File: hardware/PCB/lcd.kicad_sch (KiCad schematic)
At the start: 67 parts, among them U13 TPS923650, U14 TSC2013QRSARQ1

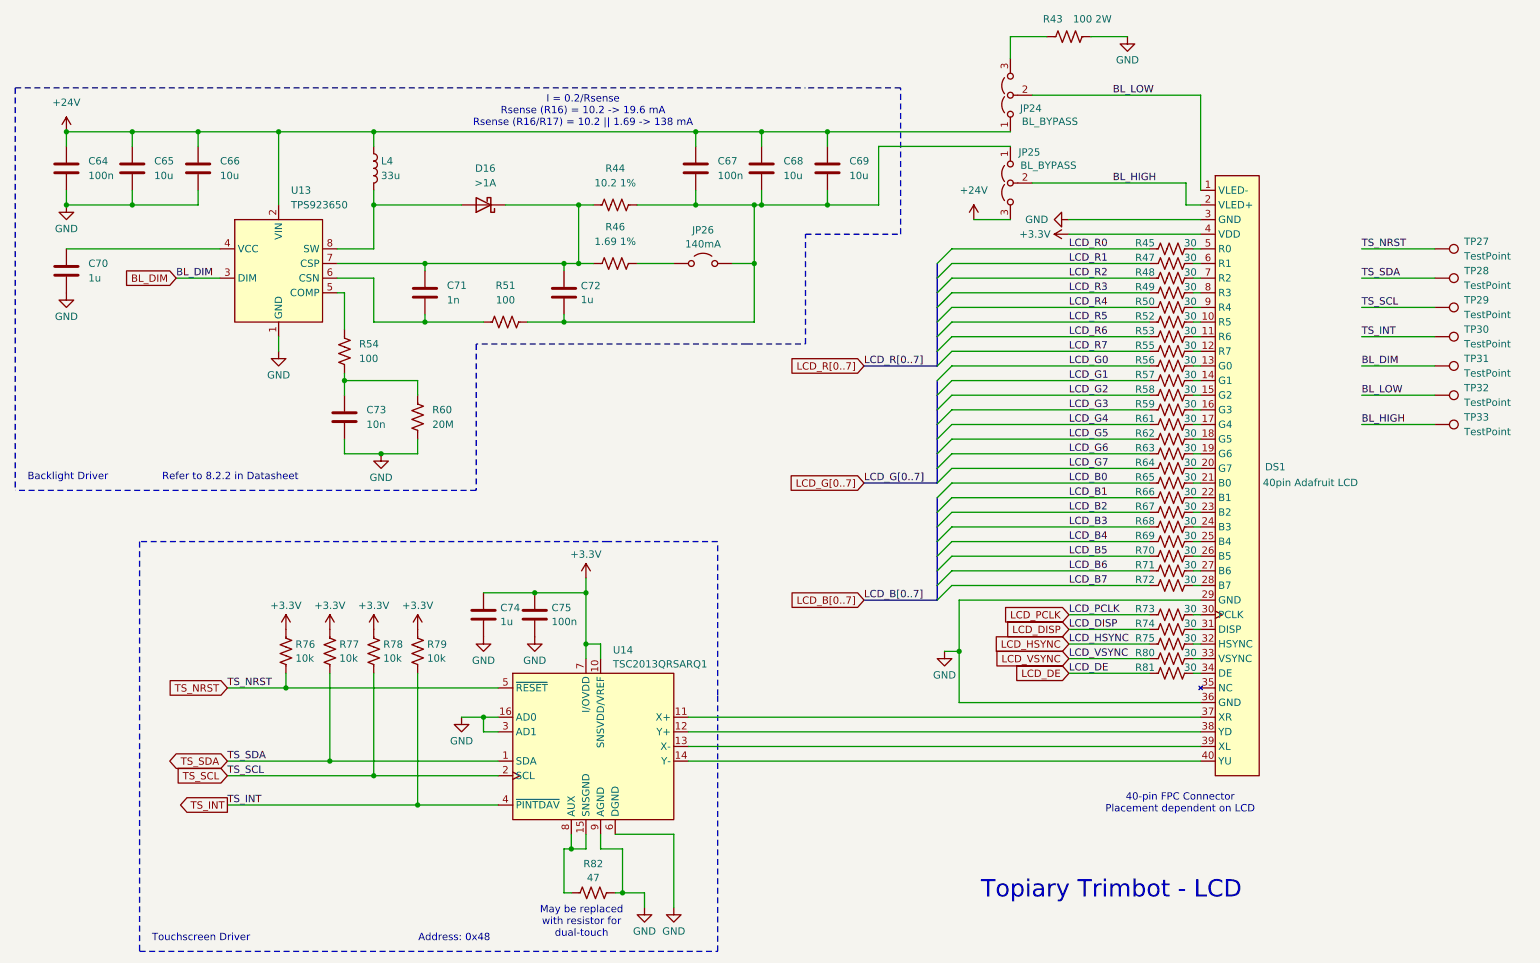
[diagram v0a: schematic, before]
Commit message: Finish first pass placement of parts on PCB, several updates and fixes to schematic included
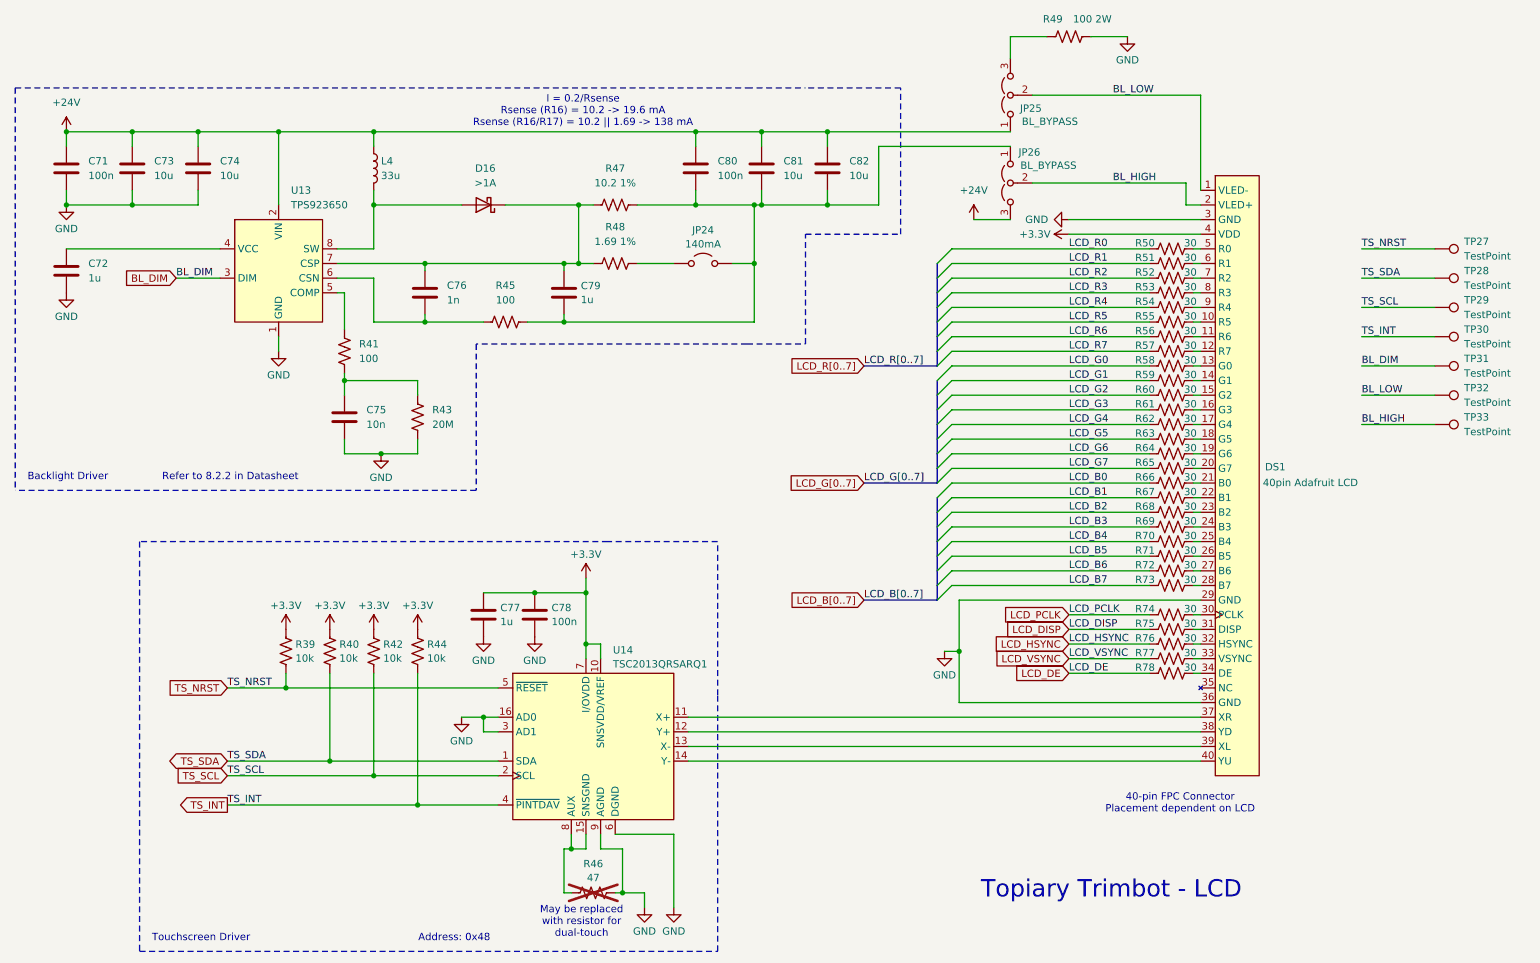
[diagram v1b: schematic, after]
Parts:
- DS1: footprint Connector_FFC-FPC:Hirose_FH12-40S-0.5SH_1x40-1MP_P0.50mm_Horizontal -> CustomFootprints:Hirose_FH12A-40S-0.5SH_1x40-1MP_P0.50mm_Horizontal
- R46: renamed from R82; now not fitted
- renumbered C64 to C71, C70 to C72, C65 to C73, C66 to C74, C73 to C75, C71 to C76, C74 to C77, C75 to C78, C72 to C79, C67 to C80, C68 to C81, C69 to C82, JP26 to JP24, JP24 to JP25, JP25 to JP26, R76 to R39, R77 to R40, R54 to R41, R78 to R42, R60 to R43, R79 to R44, R51 to R45, R44 to R47, R46 to R48, R43 to R49, R45 to R50, R47 to R51, R48 to R52, R49 to R53, R50 to R54, R52 to R55, R53 to R56, R55 to R57, R56 to R58, R57 to R59, R58 to R60, R59 to R61, R61 to R62, R62 to R63, R63 to R64, R64 to R65, R65 to R66, R66 to R67, R67 to R68, R68 to R69, R69 to R70, R70 to R71, R71 to R72, R72 to R73, R73 to R74, R74 to R75, R75 to R76, R80 to R77, R81 to R78

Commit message: Started routing
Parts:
- R46: value 47 -> 0; now fitted
- U13: footprint Package_SO:HVSSOP-8-1EP_3x3mm_P0.65mm_EP1.57x1.89mm -> CustomFootprints:TPS923650_VSSOP8
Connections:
- net GND: now also U13.9 (EP), U14.17 (EP)
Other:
- note added: "May be replaced with 47R for dual-touch"
- note removed: "May be replaced with resistor for dual-touch"

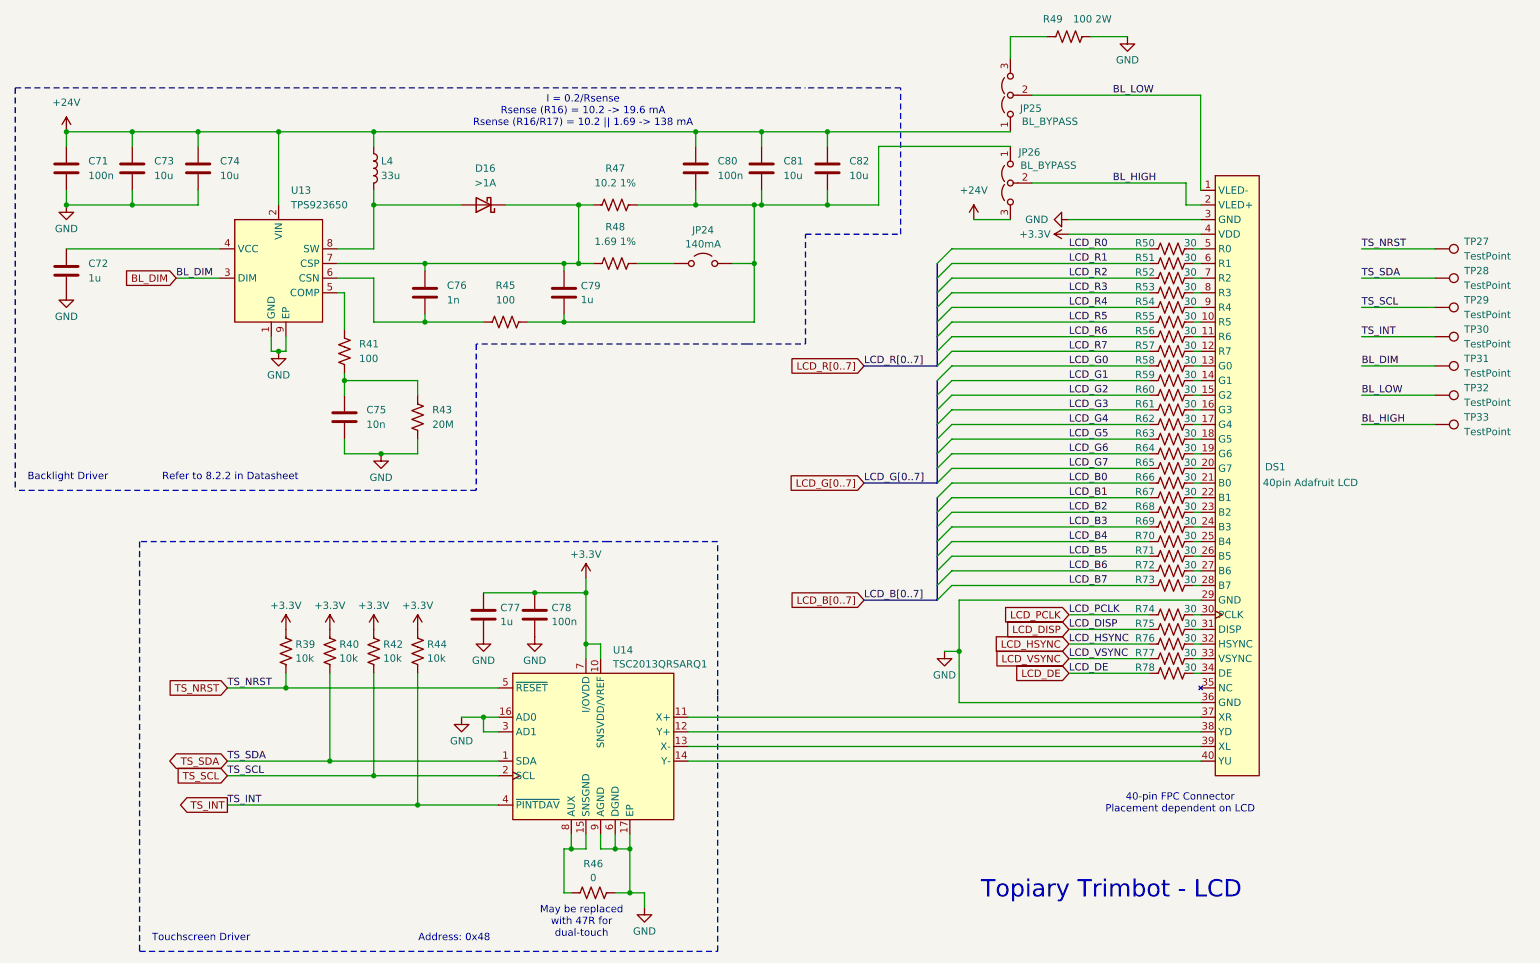
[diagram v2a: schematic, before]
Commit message: Continue layout, including swapping to linear BL driver
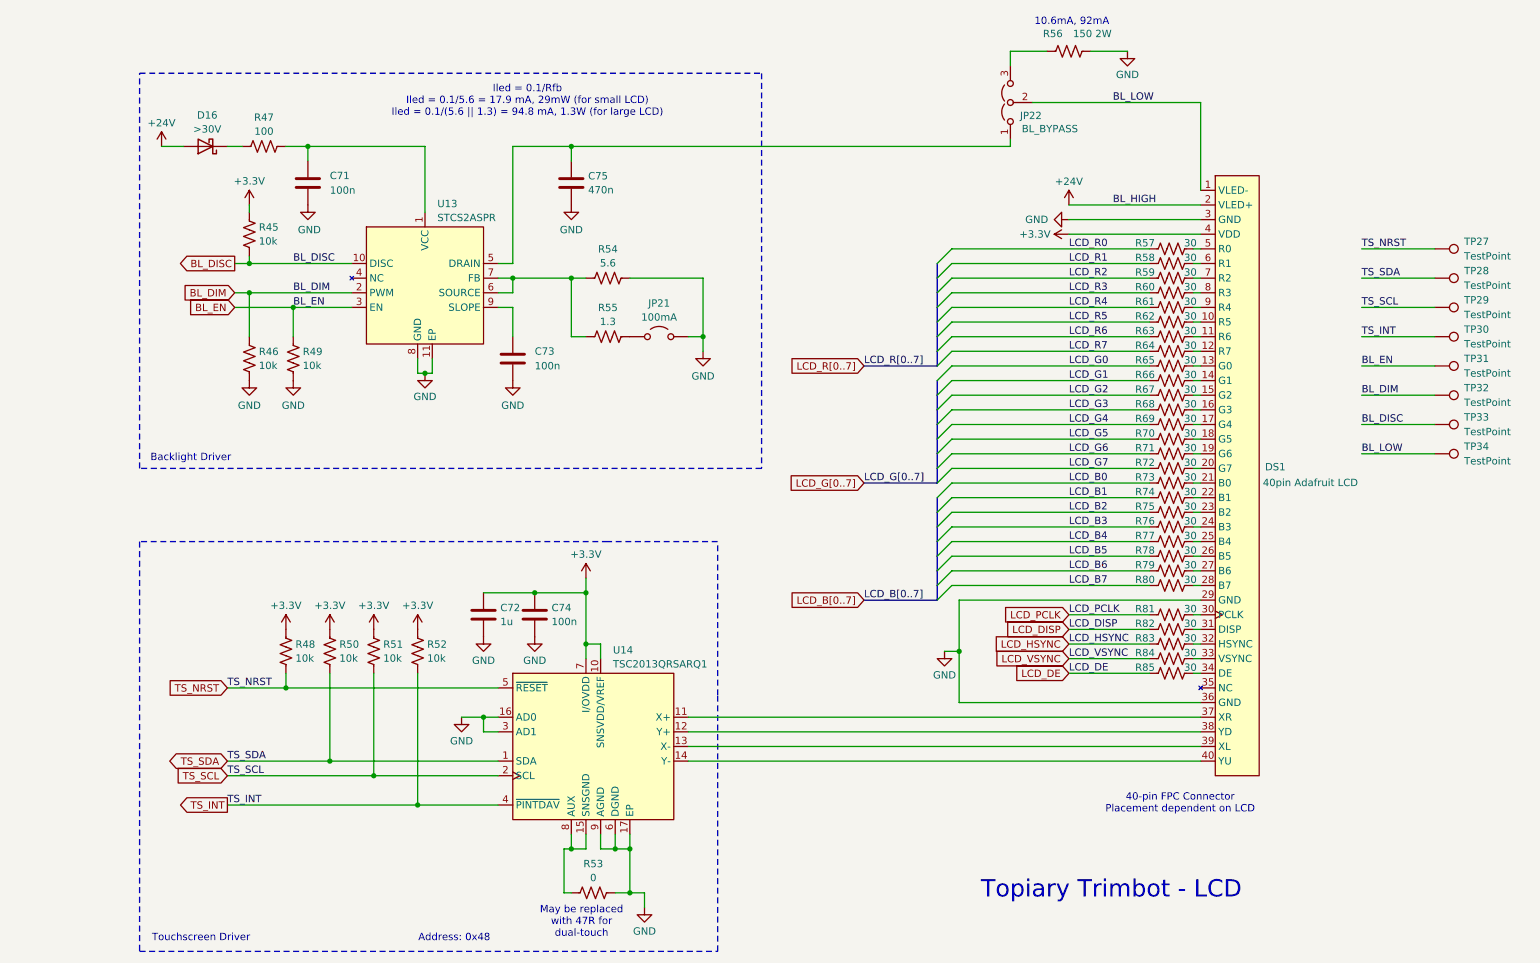
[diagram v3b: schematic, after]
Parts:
- removed C72, C79: 1u, Capacitor_SMD:C_0603_1608Metric, symbol Device:C
- removed C74, C81: 10u, Capacitor_SMD:C_0805_2012Metric, symbol Device:C
- removed C75: 10n, Capacitor_SMD:C_0603_1608Metric, symbol Device:C
- removed C76: 1n, Capacitor_SMD:C_0603_1608Metric, symbol Device:C
- removed C80: 100n, Capacitor_SMD:C_0603_1608Metric, symbol Device:C
- removed JP26: BL_BYPASS, Connector_PinHeader_2.54mm:PinHeader_1x03_P2.54mm_Vertical, symbol Jumper:Jumper_3_Open
- removed L4: 33u, Inductor_SMD:L_Bourns_SRR1208_12.7x12.7mm, symbol Device:L
- removed R41: 100, Resistor_SMD:R_0603_1608Metric, symbol Device:R_US
- removed R43: 20M, Resistor_SMD:R_0603_1608Metric, symbol Device:R_US
- removed R48: 1.69 1%, Resistor_SMD:R_0805_2012Metric, symbol Device:R_US
- removed TP33: TestPoint, TestPoint:TestPoint_Pad_D1.5mm, symbol Connector:TestPoint
- removed U13: TPS923650, CustomFootprints:TPS923650_VSSOP8, symbol CustomSymbols:TPS923650
- added R46, R49: 10k, Resistor_SMD:R_0805_2012Metric, symbol Device:R_US
- added R54: 5.6, Resistor_SMD:R_0805_2012Metric, symbol Device:R_US
- added R55: 1.3, Resistor_SMD:R_0805_2012Metric, symbol Device:R_US
- added TP31, TP32: TestPoint, TestPoint:TestPoint_Pad_D1.5mm, symbol Connector:TestPoint
- added U13: STCS2ASPR, CustomFootprints:STM_PowerSO-10, symbol CustomSymbols:STCS2ASPR
- C72: renamed from C77; footprint Capacitor_SMD:C_0603_1608Metric -> Capacitor_SMD:C_0805_2012Metric
- C73: value 10u -> 100n; footprint Capacitor_SMD:C_0805_2012Metric -> Capacitor_SMD:C_0603_1608Metric
- C75: renamed from C82; value 10u -> 470n
- D16: value >1A -> >30V; footprint Diode_SMD:D_SMB -> Diode_SMD:D_SOD-123; MANUFACTURER (none) -> STM; Manufacturer_Part_Number B280-13-F -> BAT46ZFILM
- JP21: renamed from JP24; value 140mA -> 100mA
- R45: value 100 -> 10k; footprint Resistor_SMD:R_0603_1608Metric -> Resistor_SMD:R_0805_2012Metric
- R47: value 10.2 1% -> 100
- R53: renamed from R46; footprint Resistor_SMD:R_0805_2012Metric_Pad1.20x1.40mm_HandSolder -> Resistor_SMD:R_0805_2012Metric
- R56: renamed from R49; value 100 2W -> 150 2W; Manufacturer_Part_Number AC05000001000JAC00 -> AC05000001507JAC00
- renumbered C78 to C74, JP25 to JP22, R39 to R48, R40 to R50, R42 to R51, R44 to R52, R50 to R57, R51 to R58, R52 to R59, R53 to R60, R54 to R61, R55 to R62, R56 to R63, R57 to R64, R58 to R65, R59 to R66, R60 to R67, R61 to R68, R62 to R69, R63 to R70, R64 to R71, R65 to R72, R66 to R73, R67 to R74, R68 to R75, R69 to R76, R70 to R77, R71 to R78, R72 to R79, R73 to R80, R74 to R81, R75 to R82, R76 to R83, R77 to R84, R78 to R85, TP31 to TP33, TP32 to TP34
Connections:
- net BL_HIGH is gone; now on net +24V: DS1.2 (VLED+)
- net +24V: now also D16.2 (A); no longer C71.1, C73.1, C75.1, JP22.1 (A)
- net +3.3V: now also R45.2
- net BL_DIM: now also R46.2, TP32.1, U13.2 (PWM); no longer TP33.1
- net GND: now also C75.2, JP21.2 (B), R46.1, R49.1, R54.2, U13.11 (EP), U13.8 (GND)
- net BL_DISC: now reaches R45.1
- net BL_DISC: now also TP33.1, U13.10 (DISC)
- net at JP21.1 (A): now also R55.2
- new net: R54.1, R55.1, U13.6 (SOURCE), U13.7 (FB)
- new net: C75.1, JP22.1 (A), U13.5 (DRAIN)
- new net: C71.1, R47.2, U13.1 (VCC)
- new net: C73.1, U13.9 (SLOPE)
- new net BL_EN: R49.2, TP31.1, U13.3 (EN)
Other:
- note added: "10.6mA, 92mA"
- note added: "Iled = 0.1/Rfb Iled = 0.1/5.6 = 17.9 mA, 29mW (for small LCD) Iled = 0.1/(5.6 || 1.3) = 94.8 mA, 1.3W (for large LCD)"
- note removed: "I = 0.2/Rsense"
- note removed: "Refer to 8.2.2 in Datasheet"
- note removed: "Rsense (R16) = 10.2 -> 19.6 mA Rsense (R16/R17) = 10.2 || 1.69 -> 138 mA"
- moved on the sheet: C75, JP21, JP22, R56, TP33, TP34

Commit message: all part numbers
may need revisions
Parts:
- C71, C73, C74: MANUFACTURER (none) -> Murata; Manufacturer_Part_Number (none) -> GCJ188R71H104KA12D
- C72: MANUFACTURER (none) -> Murata; Manufacturer_Part_Number (none) -> GCM21BR71E105KA56L
- C75: MANUFACTURER (none) -> Murata; Manufacturer_Part_Number (none) -> GRM21BR71H474KA88L
- DS1: MANUFACTURER (none) -> Adafruit
- JP21: MANUFACTURER (none) -> Wurth; Manufacturer_Part_Number (none) -> 61300211121
- JP22: MANUFACTURER (none) -> Wurth; Manufacturer_Part_Number (none) -> 61300311121
- R45, R46, R48, R49, R50, R51, R52: MANUFACTURER (none) -> Yageo; Manufacturer_Part_Number (none) -> RC0805JR-0710KL
- R47: MANUFACTURER (none) -> Yageo; Manufacturer_Part_Number (none) -> RC0805JR-07100RL
- R53: MANUFACTURER (none) -> Yageo; Manufacturer_Part_Number (none) -> RC0805JR-070RL
- R54: MANUFACTURER (none) -> Yageo; Manufacturer_Part_Number (none) -> RC0805FR-075R6L
- R55: MANUFACTURER (none) -> Yageo; Manufacturer_Part_Number (none) -> RC0805FR-071R3L
- R56: MANUFACTURER (none) -> Vishay
- R57, R58, R59, R60, R61, R62, R63, R64, R65, R66, R67, R68, R69, R70, R71, R72, R73, R74, R75, R76, R77, R78, R79, R80, R81, R82, R83, R84, R85: MANUFACTURER (none) -> Yageo; Manufacturer_Part_Number (none) -> RC0603FR-0730RL
- TP27, TP28, TP29, TP30, TP31, TP32, TP33, TP34: now left out of the parts list

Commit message: Update some incorrect schematic fields
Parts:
- DS1: Manufacturer_Part_Number FH12-40S-0.5SH(55) -> FH12A-40S-0.5SH(55)
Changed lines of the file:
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@@
 			)
 		)
-		(property "Manufacturer_Part_Number" "FH12-40S-0.5SH(55)"
+		(property "Manufacturer_Part_Number" "FH12A-40S-0.5SH(55)"
 			(at 228.6 104.14 0)
 			(effects
